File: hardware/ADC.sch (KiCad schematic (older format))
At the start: 21 parts, among them J4 691327310016, J5 691327310016

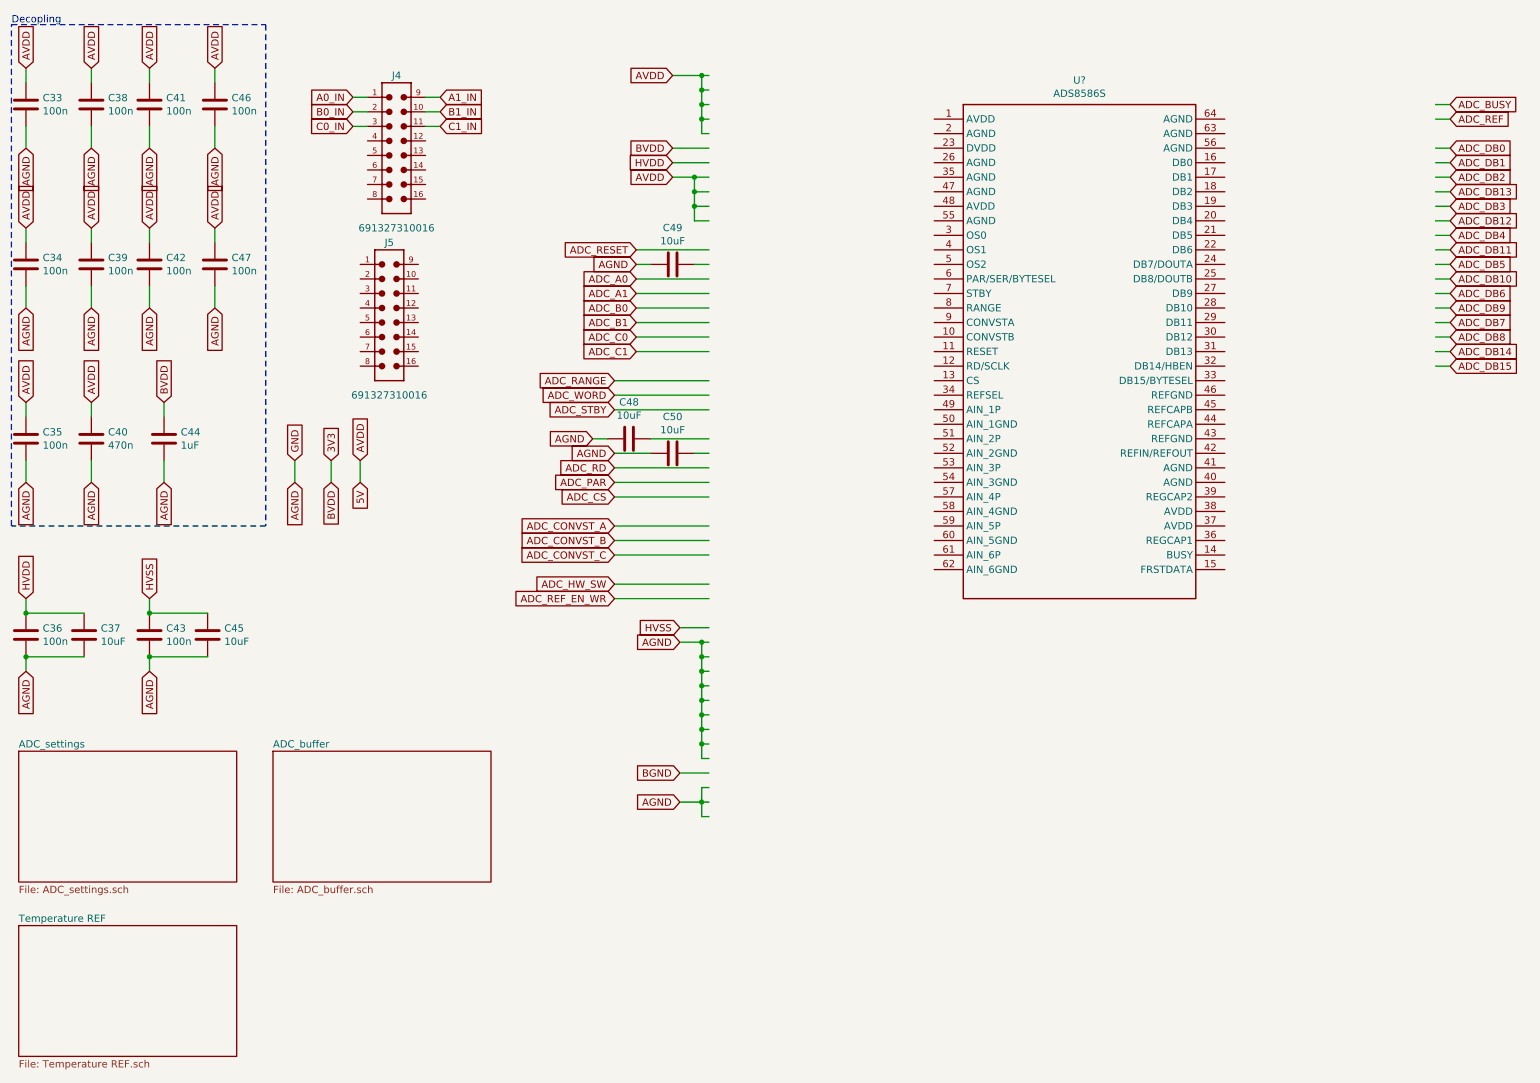
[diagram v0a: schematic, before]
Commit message: Partially connecting ads8586s
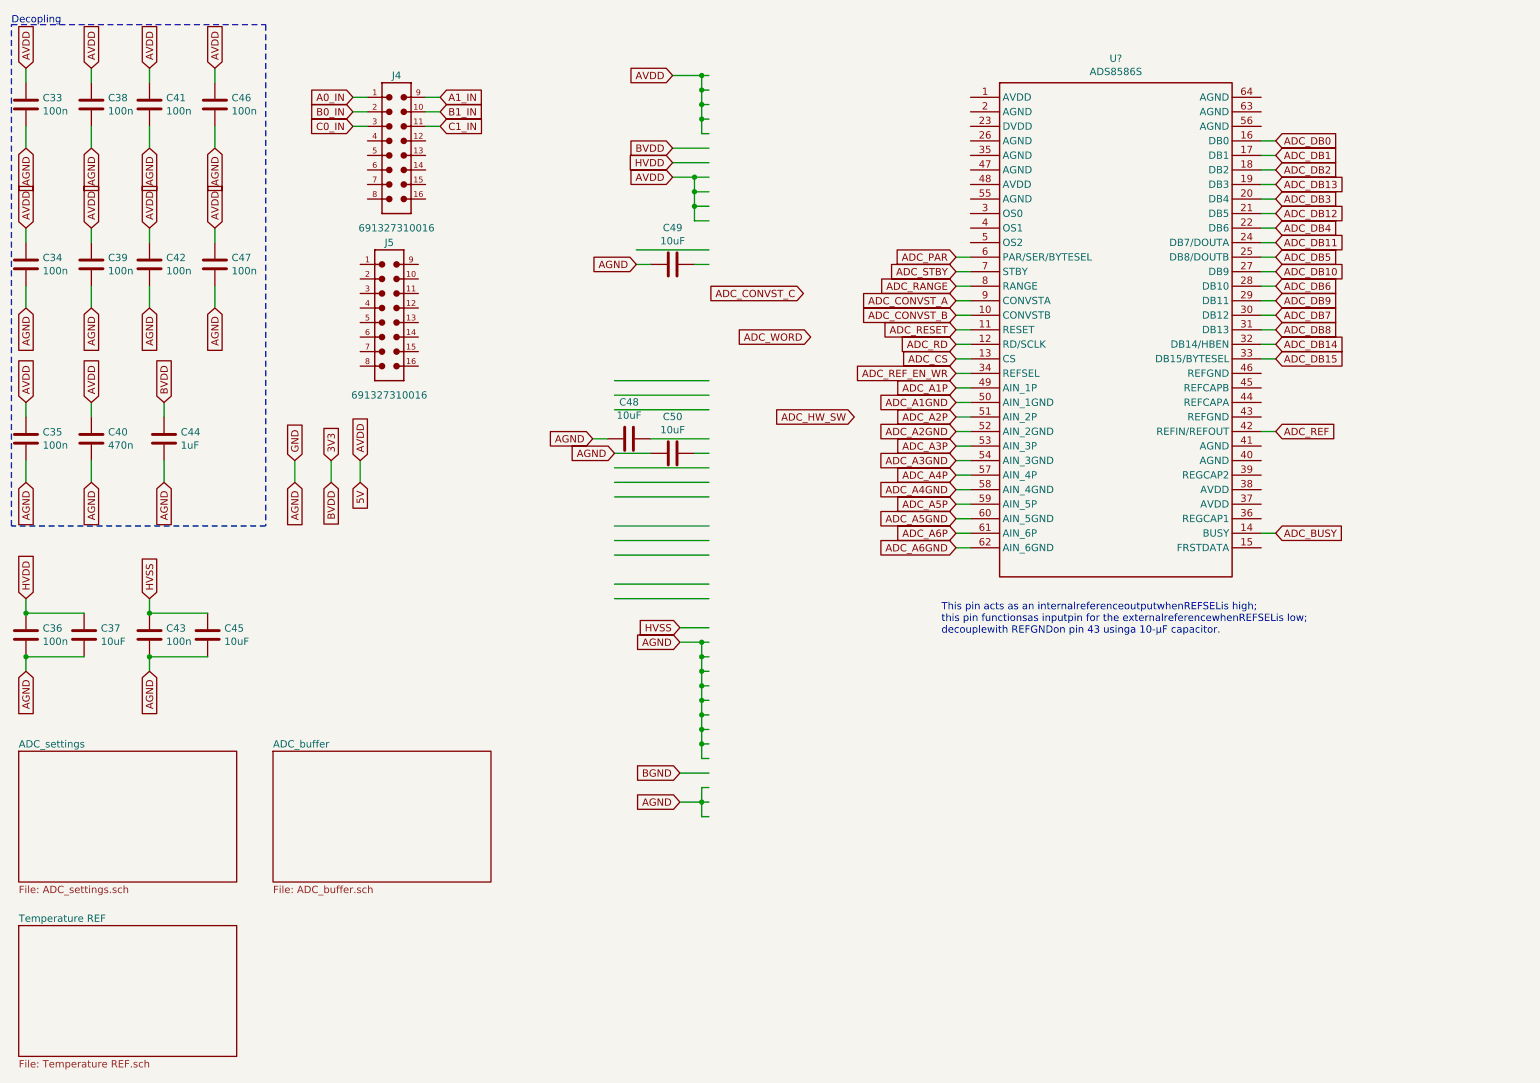
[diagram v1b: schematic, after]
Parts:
- removed U?: ADS8586S, symbol ads8586s:ADS8586S
- added U?: ADS8586S, symbol ads8586s:ADS8586S
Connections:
- net labels added: ADC_A1GND, ADC_A1P, ADC_A2GND, ADC_A2P, ADC_A3GND, ADC_A3P, ADC_A4GND, ADC_A4P, ADC_A5GND, ADC_A5P, ADC_A6GND, ADC_A6P
- net labels removed: ADC_A0, ADC_A1, ADC_B0, ADC_B1, ADC_C0, ADC_C1
- wire segments 127 -> 142
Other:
- note added: "This pin acts as an internalreferenceoutputwhenREFSELis high;\nthis pin functionsas inputpin for the externalreferencewhenREFSELis low;\ndecouplewith REFGNDon pin 43 usinga 10-μF capacitor."
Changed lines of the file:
@@
 	2100 4950 1700 4950
 Connection ~ 1700 4950
-Text GLabel 5050 2150 0    50   Input ~ 0
+Text GLabel 7250 2700 0    50   Input ~ 0
 ADC_RESET
 Wire Wire Line
 	5050 2150 5550 2150
-Text GLabel 5050 2350 0    50   Input ~ 0
-ADC_A0
-Wire Wire Line
-	5050 2350 5550 2350
-Text GLabel 5050 2450 0    50   Input ~ 0
-ADC_A1
-Text GLabel 5050 2550 0    50   Input ~ 0
-ADC_B0
-Text GLabel 5050 2650 0    50   Input ~ 0
-ADC_B1
-Text GLabel 5050 2750 0    50   Input ~ 0
-ADC_C0
-Text GLabel 5050 2850 0    50   Input ~ 0
-ADC_C1
-Wire Wire Line
-	5050 2450 5550 2450
-Wire Wire Line
-	5550 2550 5050 2550
-Wire Wire Line
-	5050 2650 5550 2650
-Wire Wire Line
-	5550 2750 5050 2750
-Wire Wire Line
-	5050 2850 5550 2850
-Text GLabel 10650 1150 2    50   Input ~ 0
+Text GLabel 7250 3100 0    50   Input ~ 0
+ADC_A1P
+Text GLabel 7250 3300 0    50   Input ~ 0
+ADC_A2P
+Text GLabel 7250 3500 0    50   Input ~ 0
+ADC_A3P
+Text GLabel 9450 4100 2    50   Input ~ 0
 ADC_BUSY
-Text GLabel 10650 1250 2    50   Input ~ 0
+Text GLabel 9450 3400 2    50   Input ~ 0
 ADC_REF
-Text GLabel 10650 1450 2    50   Input ~ 0
+Text GLabel 9450 1400 2    50   Input ~ 0
 ADC_DB0
-Text GLabel 10650 1550 2    50   Input ~ 0
+Text GLabel 9450 1500 2    50   Input ~ 0
 ADC_DB1
-Text GLabel 10650 1650 2    50   Input ~ 0
+Text GLabel 9450 1600 2    50   Input ~ 0
 ADC_DB2
-Text GLabel 10650 1750 2    50   Input ~ 0
+Text GLabel 9450 1700 2    50   Input ~ 0
 ADC_DB13
-Text GLabel 10650 1850 2    50   Input ~ 0
+Text GLabel 9450 1800 2    50   Input ~ 0
 ADC_DB3
-Text GLabel 10650 1950 2    50   Input ~ 0
+Text GLabel 9450 1900 2    50   Input ~ 0
 ADC_DB12
-Text GLabel 10650 2050 2    50   Input ~ 0
+Text GLabel 9450 2000 2    50   Input ~ 0
 ADC_DB4
-Text GLabel 10650 2150 2    50   Input ~ 0
+Text GLabel 9450 2100 2    50   Input ~ 0
 ADC_DB11
-Text GLabel 10650 2250 2    50   Input ~ 0
+Text GLabel 9450 2200 2    50   Input ~ 0
 ADC_DB5
-Text GLabel 10650 2350 2    50   Input ~ 0
+Text GLabel 9450 2300 2    50   Input ~ 0
 ADC_DB10
-Text GLabel 10650 2450 2    50   Input ~ 0
+Text GLabel 9450 2400 2    50   Input ~ 0
 ADC_DB6
-Text GLabel 10650 2550 2    50   Input ~ 0
+Text GLabel 9450 2500 2    50   Input ~ 0
 ADC_DB9
-Text GLabel 10650 2650 2    50   Input ~ 0
+Text GLabel 9450 2600 2    50   Input ~ 0
 ADC_DB7
-Text GLabel 10650 2850 2    50   Input ~ 0
+Text GLabel 9450 2800 2    50   Input ~ 0
 ADC_DB14
-Text GLabel 10650 2950 2    50   Input ~ 0
+Text GLabel 9450 2900 2    50   Input ~ 0
 ADC_DB15
-Wire Wire Line
-	10550 1150 10650 1150
-Wire Wire Line
-	10550 1250 10650 1250
-Wire Wire Line
-	10550 1450 10650 1450
-Wire Wire Line
-	10550 1550 10650 1550
-Wire Wire Line
-	10550 1650 10650 1650
-Wire Wire Line
-	10550 1750 10650 1750
-Wire Wire Line
-	10550 1850 10650 1850
-Wire Wire Line
-	10550 1950 10650 1950
-Wire Wire Line
-	10550 2050 10650 2050
-Wire Wire Line
-	10550 2150 10650 2150
-Wire Wire Line
-	10550 2250 10650 2250
-Wire Wire Line
-	10550 2350 10650 2350
-Wire Wire Line
-	10550 2450 10650 2450
-Wire Wire Line
-	10550 2550 10650 2550
-Wire Wire Line
-	10550 2650 10650 2650
-Wire Wire Line
-	10550 2850 10650 2850
-Wire Wire Line
-	10550 2950 10650 2950
-Text GLabel 10650 2750 2    50   Input ~ 0
+Text GLabel 9450 2700 2    50   Input ~ 0
 ADC_DB8
-Wire Wire Line
-	10550 2750 10650 2750
-Text GLabel 4900 3050 0    50   Input ~ 0
+Text GLabel 7250 2400 0    50   Input ~ 0
 ADC_RANGE
-Text GLabel 4900 3150 0    50   Input ~ 0
+Text GLabel 6250 2750 0    50   Input ~ 0
 ADC_WORD
-Text GLabel 4900 3250 0    50   Input ~ 0
+Text GLabel 7250 2300 0    50   Input ~ 0
 ADC_STBY
 Wire Wire Line
@@
 Wire Wire Line
 	5550 3250 4900 3250
-Text GLabel 4900 3650 0    50   Input ~ 0
+Text GLabel 7250 2800 0    50   Input ~ 0
 ADC_RD
-Text GLabel 4900 3750 0    50   Input ~ 0
+Text GLabel 7250 2200 0    50   Input ~ 0
 ADC_PAR
-Text GLabel 4900 3850 0    50   Input ~ 0
+Text GLabel 7250 2900 0    50   Input ~ 0
 ADC_CS
-Text GLabel 4900 4050 0    50   Input ~ 0
+Text GLabel 7250 2500 0    50   Input ~ 0
 ADC_CONVST_A
-Text GLabel 4900 4150 0    50   Input ~ 0
+Text GLabel 7250 2600 0    50   Input ~ 0
 ADC_CONVST_B
-Text GLabel 4900 4250 0    50   Input ~ 0
+Text GLabel 6200 2450 0    50   Input ~ 0
 ADC_CONVST_C
-Text GLabel 4900 4450 0    50   Input ~ 0
+Text GLabel 6550 3300 0    50   Input ~ 0
 ADC_HW_SW
-Text GLabel 4900 4550 0    50   Input ~ 0
+Text GLabel 7250 3000 0    50   Input ~ 0
 ADC_REF_EN_WR
 Wire Wire Line
@@
 Wire Wire Line
 	3150 3600 3150 3750
+Text Notes 7150 4800 0    50   ~ 0
+This pin acts as an internalreferenceoutputwhenREFSELis high;\nthis pin functionsas inputpin for the externalreferencewhenREFSELis low;\ndecouplewith REFGNDon pin 43 usinga 10-μF capacitor.
 $Comp
 L ads8586s:ADS8586S U?
-U 1 1 5E376959
-P 8100 2850
-F 0 "U?" H 8100 4717 50  0000 C CNN
-F 1 "ADS8586S" H 8100 4626 50  0000 C CNN
-F 2 "" H 8100 2850 50  0001 L CNN
-F 3 "" H 8100 2850 50  0001 L CNN
-	1    8100 2850
+U 1 1 5E389238
+P 8350 2700
+F 0 "U?" H 8350 4567 50  0000 C CNN
+F 1 "ADS8586S" H 8350 4476 50  0000 C CNN
+F 2 "" H 8350 2700 50  0001 L CNN
+F 3 "" H 8350 2700 50  0001 L CNN
+	1    8350 2700
 	1    0    0    -1
 $EndComp
+Wire Wire Line
+	9350 1400 9450 1400
+Wire Wire Line
+	9350 1500 9450 1500
+Wire Wire Line
+	9350 1600 9450 1600
+Wire Wire Line
+	9350 1700 9450 1700
+Wire Wire Line
+	9350 1800 9450 1800
+Wire Wire Line
+	9350 1900 9450 1900
+Wire Wire Line
+	9350 2000 9450 2000
+Wire Wire Line
+	9350 2100 9450 2100
+Wire Wire Line
+	9350 2200 9450 2200
+Wire Wire Line
+	9350 2300 9450 2300
+Wire Wire Line
+	9350 2400 9450 2400
+Wire Wire Line
+	9350 2500 9450 2500
+Wire Wire Line
+	9350 2600 9450 2600
+Wire Wire Line
+	9350 2700 9450 2700
+Wire Wire Line
+	9350 2800 9450 2800
+Wire Wire Line
+	9350 2900 9450 2900
+Wire Wire Line
+	9350 3400 9450 3400
+Wire Wire Line
+	9350 4100 9450 4100
+Text GLabel 7250 3200 0    50   Input ~ 0
+ADC_A1GND
+Text GLabel 7250 3400 0    50   Input ~ 0
+ADC_A2GND
+Text GLabel 7250 3600 0    50   Input ~ 0
+ADC_A3GND
+Text GLabel 7250 3700 0    50   Input ~ 0
+ADC_A4P
+Text GLabel 7250 3800 0    50   Input ~ 0
+ADC_A4GND
+Text GLabel 7250 3900 0    50   Input ~ 0
+ADC_A5P
+Text GLabel 7250 4000 0    50   Input ~ 0
+ADC_A5GND
+Text GLabel 7250 4100 0    50   Input ~ 0
+ADC_A6P
+Text GLabel 7250 4200 0    50   Input ~ 0
+ADC_A6GND
+Wire Wire Line
+	7250 3100 7350 3100
+Wire Wire Line
+	7250 3200 7350 3200
+Wire Wire Line
+	7250 3300 7350 3300
+Wire Wire Line
+	7250 3400 7350 3400
+Wire Wire Line
+	7250 3500 7350 3500
+Wire Wire Line
+	7250 3600 7350 3600
+Wire Wire Line
+	7250 3700 7350 3700
+Wire Wire Line
+	7250 3800 7350 3800
+Wire Wire Line
+	7250 3900 7350 3900
+Wire Wire Line
+	7250 4000 7350 4000
+Wire Wire Line
+	7250 4100 7350 4100
+Wire Wire Line
+	7250 4200 7350 4200
+Wire Wire Line
+	7250 3000 7350 3000
+Wire Wire Line
+	7250 2900 7350 2900
+Wire Wire Line
+	7250 2800 7350 2800
+Wire Wire Line
+	7250 2700 7350 2700
+Wire Wire Line
+	7250 2600 7350 2600
+Wire Wire Line
+	7250 2500 7350 2500
+Wire Wire Line
+	7250 2400 7350 2400
+Wire Wire Line
+	7250 2300 7350 2300
+Wire Wire Line
+	7250 2200 7350 2200
 $EndSCHEMATC

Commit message: Adding last known changes to shematics
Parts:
- removed C36, C41, C42, C43, C46, C47: 100n, Capacitor_SMD:C_0603_1608Metric, symbol antena:C
- removed C37, C45, C48, C49, C50: 10uF, Capacitor_SMD:C_0603_1608Metric, symbol antena:C
- removed C44: 1uF, Capacitor_SMD:C_0603_1608Metric, symbol antena:C
- added C? (x2): 10uF, symbol antena:CP
- added C?: 10uF, Capacitor_SMD:C_0603_1608Metric, symbol antena:C
- added C?: 1u/X7R-grade, Capacitor_SMD:C_0603_1608Metric, symbol antena:C
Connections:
- net labels added: A2_IN, A3_IN, A4_IN, A5_IN, A6_IN, ADC_FRSTDATA, ADC_REFGND, DVDD, OS0, OS1, OS2
- net labels removed: A0_IN, ADC_CONVST_C, ADC_HW_SW, ADC_WORD, B0_IN, B1_IN, BGND, BVDD, C0_IN, C1_IN, HVDD, HVSS
- wire segments 142 -> 96
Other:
- moved on the sheet: C34, C35, C39, C40, U?

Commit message: Routing board
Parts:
- removed C40: 470n, Capacitor_SMD:C_0603_1608Metric, symbol antena:C
- C26, C29: renamed from C?; footprint (none) -> Capacitor_SMD:C_0805_2012Metric
- C27, C28: renamed from C?; footprint Capacitor_SMD:C_0603_1608Metric -> Capacitor_SMD:C_0805_2012Metric
- U1: renamed from U?; footprint (none) -> Package_QFP:LQFP-64_10x10mm_P0.5mm
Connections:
- net ADC_A2GND is gone; now on net ADC_REFGND: U1.52 (AIN_2GND)
- net ADC_A3GND is gone; now on net ADC_REFGND: U1.54 (AIN_3GND)
- net ADC_REFGND: no longer U1.47 (AGND)
- net A2_IN renamed A2_IN_P
- net A3_IN renamed A2_IN_N
- net A4_IN renamed A4_IN_P
- net A5_IN renamed A4_IN_N
- net ADC_A2P renamed ADC_A2_OUT_P
- net ADC_A3P renamed ADC_A2_OUT_N
- net ADC_A4P renamed ADC_A4_OUT_P
- net ADC_A5P renamed ADC_A4_OUT_N
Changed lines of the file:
@@
 Wire Wire Line
 	850  2450 850  2600
-Text GLabel 1300 2050 1    50   Input ~ 0
-AVDD
-Text GLabel 1300 2600 3    50   Input ~ 0
-AGND
-$Comp
-L antena:C C40
-U 1 1 5E31DDD7
-P 1300 2300
-F 0 "C40" H 1415 2346 50  0000 L CNN
-F 1 "470n" H 1415 2255 50  0000 L CNN
-F 2 "Capacitor_SMD:C_0603_1608Metric" H 1338 2150 50  0001 C CNN
-F 3 "~" H 1300 2300 50  0001 C CNN
-	1    1300 2300
-	1    0    0    -1
-$EndComp
-Wire Wire Line
-	1300 2050 1300 2150
-Wire Wire Line
-	1300 2450 1300 2600
 Text GLabel 5100 2750 0    50   Input ~ 0
 ADC_RESET
@@
 ADC_A1P
 Text GLabel 5100 3350 0    50   Input ~ 0
-ADC_A2P
+ADC_A2_OUT_P
 Text GLabel 5100 3550 0    50   Input ~ 0
-ADC_A3P
+ADC_A2_OUT_N
 Text GLabel 7300 4150 2    50   Input ~ 0
 ADC_BUSY
@@
 A1_IN
 Text GLabel 3100 1200 0    50   Input ~ 0
-A2_IN
+A2_IN_P
 Wire Wire Line
 	3600 1100 3700 1100
@@
 	3100 1100 3200 1100
 Text GLabel 3700 1200 2    50   Input ~ 0
-A3_IN
+A2_IN_N
 Text GLabel 3100 1300 0    50   Input ~ 0
-A4_IN
+A4_IN_P
 Wire Wire Line
 	3700 1200 3600 1200
@@
 	3100 1200 3200 1200
 Text GLabel 3700 1300 2    50   Input ~ 0
-A5_IN
+A4_IN_N
 Text GLabel 3100 1400 0    50   Input ~ 0
 A6_IN
@@
 This pin acts as an internalreferenceoutputwhenREFSELis high;\nthis pin functionsas inputpin for the externalreferencewhenREFSELis low;\ndecouplewith REFGNDon pin 43 usinga 10-μF capacitor.
 $Comp
-L ads8586s:ADS8586S U?
+L ads8586s:ADS8586S U1
 U 1 1 5E389238
 P 6200 2750
-F 0 "U?" H 6200 4617 50  0000 C CNN
+F 0 "U1" H 6200 4617 50  0000 C CNN
 F 1 "ADS8586S" H 6200 4526 50  0000 C CNN
-F 2 "" H 6200 2750 50  0001 L CNN
+F 2 "Package_QFP:LQFP-64_10x10mm_P0.5mm" H 6200 2750 50  0001 L CNN
 F 3 "" H 6200 2750 50  0001 L CNN
 	1    6200 2750
@@
 	7200 4150 7300 4150
 Text GLabel 5100 3750 0    50   Input ~ 0
-ADC_A4P
+ADC_A4_OUT_P
 Text GLabel 5100 3950 0    50   Input ~ 0
-ADC_A5P
+ADC_A4_OUT_N
 Text GLabel 5100 4150 0    50   Input ~ 0
 ADC_A6P
@@
 Text GLabel 8500 1950 3    50   Input ~ 0
 ADC_REFGND
-Text GLabel 7300 3350 2    50   Input ~ 0
-ADC_REFGND
 Text GLabel 7300 3450 2    50   Input ~ 0
 ADC_REF
@@
 	8500 1800 8500 1950
 $Comp
-L antena:CP C?
+L antena:CP C29
 U 1 1 5E4C26BA
 P 8500 1650
-F 0 "C?" H 8618 1696 50  0000 L CNN
+F 0 "C29" H 8618 1696 50  0000 L CNN
 F 1 "10uF" H 8618 1605 50  0000 L CNN
-F 2 "" H 8538 1500 50  0001 C CNN
+F 2 "Capacitor_SMD:C_0805_2012Metric" H 8538 1500 50  0001 C CNN
 F 3 "~" H 8500 1650 50  0001 C CNN
 	1    8500 1650
@@
 	7350 3250 7200 3250
 $Comp
-L antena:CP C?
+L antena:CP C26
 U 1 1 5E4CB29C
 P 7950 3200
-F 0 "C?" V 8205 3200 50  0000 C CNN
+F 0 "C26" V 8205 3200 50  0000 C CNN
 F 1 "10uF" V 8114 3200 50  0000 C CNN
-F 2 "" H 7988 3050 50  0001 C CNN
+F 2 "Capacitor_SMD:C_0805_2012Metric" H 7988 3050 50  0001 C CNN
 F 3 "~" H 7950 3200 50  0001 C CNN
 	1    7950 3200
@@
 Text GLabel 8300 1600 1    50   Input ~ 0
 ADC_REFGND
-Text GLabel 8300 1750 3    50   Input ~ 0
-GND
-Wire Wire Line
-	8300 1600 8300 1750
 Text GLabel 7300 3550 2    50   Input ~ 0
 GND
@@
 	7200 1350 7300 1350
 Wire Wire Line
-	5050 1450 5200 1450
-Wire Wire Line
 	5050 1550 5200 1550
-Wire Wire Line
-	5050 1650 5200 1650
 Wire Wire Line
 	5050 1850 5200 1850
@@
 	7200 3850 7350 3850
 $Comp
-L antena:C C?
+L antena:C C28
 U 1 1 5E5BB185
 P 8000 4050
-F 0 "C?" H 8115 4096 50  0000 L CNN
+F 0 "C28" H 8115 4096 50  0000 L CNN
 F 1 "10uF" H 8300 4300 50  0000 L CNN
-F 2 "Capacitor_SMD:C_0603_1608Metric" H 8038 3900 50  0001 C CNN
+F 2 "Capacitor_SMD:C_0805_2012Metric" H 8038 3900 50  0001 C CNN
 F 3 "~" H 8000 4050 50  0001 C CNN
 	1    8000 4050
@@
 $EndComp
 $Comp
-L antena:C C?
+L antena:C C27
 U 1 1 5E5BB33B
 P 8000 3750
-F 0 "C?" H 8115 3796 50  0000 L CNN
+F 0 "C27" H 8115 3796 50  0000 L CNN
 F 1 "1u/X7R-grade" V 7850 3500 50  0000 L CNN
-F 2 "Capacitor_SMD:C_0603_1608Metric" H 8038 3600 50  0001 C CNN
+F 2 "Capacitor_SMD:C_0805_2012Metric" H 8038 3600 50  0001 C CNN
 F 3 "~" H 8000 3750 50  0001 C CNN
 	1    8000 3750
@@
 Text GLabel 5050 1250 0    50   Input ~ 0
 AGND
-Text GLabel 5050 1450 0    50   Input ~ 0
-AGND
 Text GLabel 5050 1550 0    50   Input ~ 0
-AGND
-Text GLabel 5050 1650 0    50   Input ~ 0
 AGND
 Text GLabel 5050 1850 0    50   Input ~ 0
@@
 Text GLabel 5100 3250 0    50   Input ~ 0
 ADC_A1GND
-Text GLabel 5100 3450 0    50   Input ~ 0
-ADC_A2GND
-Text GLabel 5100 3650 0    50   Input ~ 0
-ADC_A3GND
 Text GLabel 5100 3850 0    50   Input ~ 0
 ADC_A4GND
@@
 Text GLabel 5100 4250 0    50   Input ~ 0
 ADC_A6GND
+Text GLabel 5100 3650 0    50   Input ~ 0
+AGND
+Text GLabel 5100 3450 0    50   Input ~ 0
+AGND
+Text GLabel 7300 3350 2    50   Input ~ 0
+AGND
+Text GLabel 8300 1750 3    50   Input ~ 0
+AGND
+Wire Wire Line
+	8300 1600 8300 1750
+$Comp
+L EEZ_DIB_MCU_r1B1-eagle-import:GND #SUPPLY?
+U 1 1 5E40527A
+P 3200 3850
+AR Path="/5E22C01C/5E40527A" Ref="#SUPPLY?"  Part="1"
+AR Path="/5E22D897/5E40527A" Ref="#SUPPLY0114"  Part="1"
+F 0 "#SUPPLY0114" H 3200 3850 50  0001 C CNN
+F 1 "GND" H 3200 3720 59  0000 C CNN
+F 2 "" H 3200 3850 50  0001 C CNN
+F 3 "" H 3200 3850 50  0001 C CNN
+	1    3200 3850
+	1    0    0    -1
+$EndComp
+Text GLabel 3200 3650 1    50   Input ~ 0
+GND
+Wire Wire Line
+	3200 3650 3200 3750
+$Comp
+L EEZ_DIB_MCU_r1B1-eagle-import:GND #SUPPLY?
+U 1 1 5E41D834
+P 4600 1650
+AR Path="/5E22C01C/5E41D834" Ref="#SUPPLY?"  Part="1"
+AR Path="/5E22D897/5E41D834" Ref="#SUPPLY?"  Part="1"
+F 0 "#SUPPLY?" H 4600 1650 50  0001 C CNN
+F 1 "GND" V 4600 1572 59  0000 R CNN
+F 2 "" H 4600 1650 50  0001 C CNN
+F 3 "" H 4600 1650 50  0001 C CNN
+	1    4600 1650
+	0    1    1    0
+$EndComp
+Wire Wire Line
+	4700 1650 5200 1650
+Text GLabel 4600 1450 0    50   Input ~ 0
+GND
+Wire Wire Line
+	4600 1450 5200 1450
 $EndSCHEMATC
